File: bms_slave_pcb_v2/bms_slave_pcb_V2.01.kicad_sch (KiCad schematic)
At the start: 3 parts, among them J1 isoSPI Daisy Chain IN, J2 isoSPI Daisy Chain OUT, U1 LTC6811HGI-1I-3ZZTRPBF

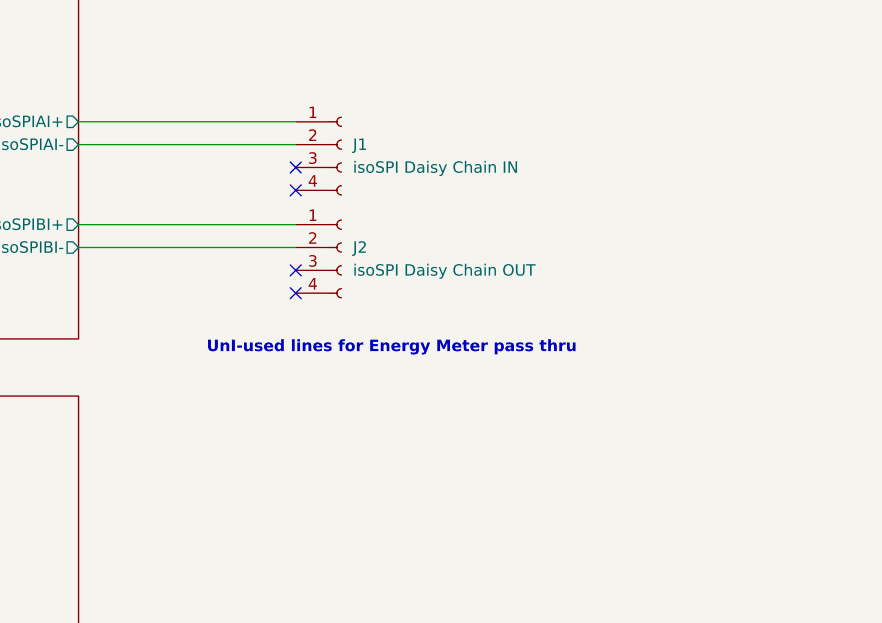
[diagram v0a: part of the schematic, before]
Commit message: Fixed filenames in BMS Slave PCB V2.01, added equipment wishlist
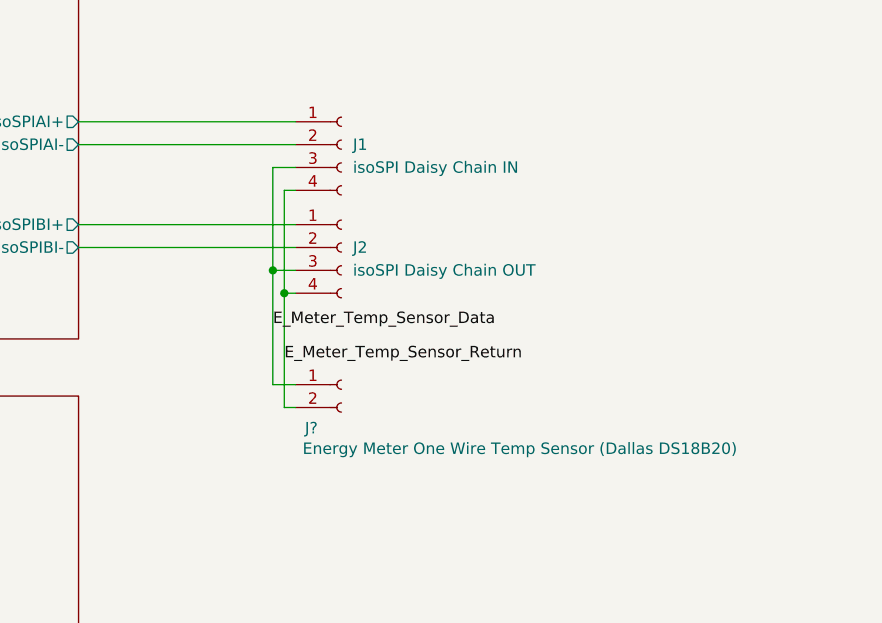
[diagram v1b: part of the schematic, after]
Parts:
- added J?: Energy Meter One Wire Temp Sensor (Dallas DS18B20), symbol Connector:Conn_01x02_Socket
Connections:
- net E_Meter_Temp_Sensor_Data: now reaches J1.3 (Pin_3)
- net E_Meter_Temp_Sensor_Data: now also J2.3 (Pin_3), J?.1 (Pin_1)
- net E_Meter_Temp_Sensor_Return: now reaches J1.4 (Pin_4)
- net E_Meter_Temp_Sensor_Return: now also J2.4 (Pin_4), J?.2 (Pin_2)
- no-connect marks 7 -> 3
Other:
- note removed: "UnI-used lines for Energy Meter pass thru"
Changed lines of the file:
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@@
 		)
 	)
-	(text "UnI-used lines for Energy Meter pass thru"
-		(exclude_from_sim no)
-		(at 348.488 124.206 0)
-		(effects
-			(font
-				(size 1.27 1.27)
-				(thickness 0.254)
-				(bold yes)
-			)
-		)
-	)
 	(text "Just as a note for ALL component footprints:\nI- make ALL caps 0805 handsolder (except voltage tap ones)\nI- make any resistor dealing with signal logic 0603 handsolder\nI- make any resistor carrying high current >=0805\nI- try to find handsolder footprint versions of any other component"
 		(exclude_from_sim no)
@@
 	)
 	(junction
+		(at 336.55 118.11)
+		(diameter 0)
+		(color 0 0 0 0)
+	)
+	(junction
+		(at 335.28 115.57)
+		(diameter 0)
+		(color 0 0 0 0)
+	)
+	(junction
 		(at 243.84 139.7)
 		(diameter 0)
@@
 	)
 	(no_connect
-		(at 337.82 106.68)
-	)
-	(no_connect
-		(at 337.82 115.57)
-	)
-	(no_connect
-		(at 337.82 118.11)
-	)
-	(no_connect
 		(at 226.06 114.3)
 	)
-	(no_connect
-		(at 337.82 104.14)
+	(wire
+		(pts
+			(xy 337.82 104.14) (xy 335.28 104.14)
+		)
+		(stroke
+			(width 0)
+			(type default)
+		)
 	)
 	(wire
@@
 	(wire
 		(pts
+			(xy 335.28 104.14) (xy 335.28 115.57)
+		)
+		(stroke
+			(width 0)
+			(type default)
+		)
+	)
+	(wire
+		(pts
 			(xy 100.33 128.27) (xy 109.22 128.27)
 		)
@@
 	(wire
 		(pts
+			(xy 336.55 118.11) (xy 337.82 118.11)
+		)
+		(stroke
+			(width 0)
+			(type default)
+		)
+	)
+	(wire
+		(pts
 			(xy 175.26 162.56) (xy 180.34 162.56)
 		)
@@
 	(wire
 		(pts
+			(xy 335.28 128.27) (xy 337.82 128.27)
+		)
+		(stroke
+			(width 0)
+			(type default)
+		)
+	)
+	(wire
+		(pts
 			(xy 175.26 142.24) (xy 180.34 142.24)
 		)
@@
 	(wire
 		(pts
+			(xy 335.28 115.57) (xy 335.28 128.27)
+		)
+		(stroke
+			(width 0)
+			(type default)
+		)
+	)
+	(wire
+		(pts
 			(xy 228.6 106.68) (xy 228.6 82.55)
 		)
@@
 	(wire
 		(pts
+			(xy 335.28 115.57) (xy 337.82 115.57)
+		)
+		(stroke
+			(width 0)
+			(type default)
+		)
+	)
+	(wire
+		(pts
 			(xy 175.26 119.38) (xy 180.34 119.38)
 		)
@@
 	(wire
 		(pts
+			(xy 337.82 106.68) (xy 336.55 106.68)
+		)
+		(stroke
+			(width 0)
+			(type default)
+		)
+	)
+	(wire
+		(pts
 			(xy 276.86 189.23) (xy 69.85 189.23)
 		)
@@
 	(wire
 		(pts
+			(xy 336.55 130.81) (xy 337.82 130.81)
+		)
+		(stroke
+			(width 0)
+			(type default)
+		)
+	)
+	(wire
+		(pts
 			(xy 59.69 199.39) (xy 59.69 120.65)
 		)
@@
 	(wire
 		(pts
+			(xy 336.55 118.11) (xy 336.55 130.81)
+		)
+		(stroke
+			(width 0)
+			(type default)
+		)
+	)
+	(wire
+		(pts
 			(xy 175.26 144.78) (xy 180.34 144.78)
 		)
@@
 	(wire
 		(pts
+			(xy 336.55 106.68) (xy 336.55 118.11)
+		)
+		(stroke
+			(width 0)
+			(type default)
+		)
+	)
+	(wire
+		(pts
 			(xy 226.06 160.02) (xy 229.87 160.02)
 		)
@@
 		)
 	)
+	(label "E_Meter_Temp_Sensor_Return"
+		(at 336.55 125.73 0)
+		(effects
+			(font
+				(size 1.27 1.27)
+			)
+			(justify left bottom)
+		)
+	)
+	(label "E_Meter_Temp_Sensor_Data"
+		(at 335.28 121.92 0)
+		(effects
+			(font
+				(size 1.27 1.27)
+			)
+			(justify left bottom)
+		)
+	)
 	(symbol
 		(lib_id "BYU_LIBRARY:LTC6811HG-1-3ZZTRPBF")
@@
 		)
 		(instances
-			(project "bms_slave_pcb"
+			(project "bms_slave_pcb_V2.01"
 				(path "/41ccf350-ee7b-4386-b0cf-c25b52556b27"
 					(reference "U1")
@@
 		)
 		(instances
-			(project "bms_slave_pcb"
+			(project "bms_slave_pcb_V2.01"
 				(path "/41ccf350-ee7b-4386-b0cf-c25b52556b27"
 					(reference "J1")
@@
 	)
 	(symbol
+		(lib_id "Connector:Conn_01x02_Socket")
+		(at 342.9 128.27 0)
+		(unit 1)
+		(body_style 1)
+		(exclude_from_sim no)
+		(in_bom yes)
+		(on_board yes)
+		(in_pos_files yes)
+		(dnp no)
+		(property "Reference" "J?"
+			(at 338.836 133.096 0)
+			(show_name no)
+			(do_not_autoplace no)
+			(effects
+				(font
+					(size 1.27 1.27)
+				)
+				(justify left)
+			)
+		)
+		(property "Value" "Energy Meter One Wire Temp Sensor (Dallas DS18B20)"
+			(at 338.582 135.382 0)
+			(show_name no)
+			(do_not_autoplace no)
+			(effects
+				(font
+					(size 1.27 1.27)
+				)
+				(justify left)
+			)
+		)
+		(property "Footprint" ""
+			(at 342.9 128.27 0)
+			(hide yes)
+			(show_name no)
+			(do_not_autoplace no)
+			(effects
+				(font
+					(size 1.27 1.27)
+				)
+			)
+		)
+		(property "Datasheet" ""
+			(at 342.9 128.27 0)
+			(hide yes)
+			(show_name no)
+			(do_not_autoplace no)
+			(effects
+				(font
+					(size 1.27 1.27)
+				)
+			)
+		)
+		(property "Description" "Generic connector, single row, 01x02, script generated"
+			(at 342.9 128.27 0)
+			(hide yes)
+			(show_name no)
+			(do_not_autoplace no)
+			(effects
+				(font
+					(size 1.27 1.27)
+				)
+			)
+		)
+		(pin "2"
+		)
+		(pin "1"
+		)
+		(instances
+			(project "bms_slave_pcb_V2.01"
+				(path "/41ccf350-ee7b-4386-b0cf-c25b52556b27"
+					(reference "J?")
+					(unit 1)
+				)
+			)
+		)
+	)
+	(symbol
 		(lib_id "power:GNDREF")
 		(at 228.6 148.59 90)
@@
 		)
 		(instances
-			(project "bms_slave_pcb"
+			(project "bms_slave_pcb_V2.01"
 				(path "/41ccf350-ee7b-4386-b0cf-c25b52556b27"
 					(reference "#PWR01")
@@
 		)
 		(instances
-			(project "bms_slave_pcb"
+			(project "bms_slave_pcb_V2.01"
 				(path "/41ccf350-ee7b-4386-b0cf-c25b52556b27"
 					(reference "J2")
@@
 		)
 		(instances
-			(project "bms_slave_pcb"
+			(project "bms_slave_pcb_V2.01"
 				(path "/41ccf350-ee7b-4386-b0cf-c25b52556b27"
 					(page "2")
@@
 		)
 		(instances
-			(project "bms_slave_pcb"
+			(project "bms_slave_pcb_V2.01"
 				(path "/41ccf350-ee7b-4386-b0cf-c25b52556b27"
 					(page "6")
@@
 		)
 		(instances
-			(project "bms_slave_pcb"
+			(project "bms_slave_pcb_V2.01"
 				(path "/41ccf350-ee7b-4386-b0cf-c25b52556b27"
 					(page "5")
@@
 		)
 		(instances
-			(project "bms_slave_pcb"
+			(project "bms_slave_pcb_V2.01"
 				(path "/41ccf350-ee7b-4386-b0cf-c25b52556b27"
 					(page "7")
@@
 		)
 		(instances
-			(project "bms_slave_pcb"
+			(project "bms_slave_pcb_V2.01"
 				(path "/41ccf350-ee7b-4386-b0cf-c25b52556b27"
 					(page "3")
